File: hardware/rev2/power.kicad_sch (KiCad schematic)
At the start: 22 parts, among them J8 Battery Connection, U5 MP2664GG-xxxx-P, U6 MAX17055ETB+, U8 TPS631000DRLR

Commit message: changed layout a bit, updated footprints, did stuff
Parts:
- added C55: 100 nF, Capacitor_SMD:C_0603_1608Metric_Pad1.08x0.95mm_HandSolder, symbol Device:C
- U8: footprint TPS631000DRLR_TEX -> _footprints:TPS631000DRLR_TEX
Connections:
- net +3V3: now also C55.1
- net BATT+: now also J8.1 (Pin_1); no longer J8.3 (Pin_3)
- net BATT-: now also J8.3 (Pin_3); no longer J8.1 (Pin_1)
- net GND: now also C55.2
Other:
- moved on the sheet: J8
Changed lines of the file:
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@@
 	)
 	(junction
-		(at 215.9 49.53)
-		(diameter 0)
-		(color 0 0 0 0)
-	)
-	(junction
 		(at 137.16 130.81)
 		(diameter 0)
@@
 	)
 	(junction
+		(at 228.6 49.53)
+		(diameter 0)
+		(color 0 0 0 0)
+	)
+	(junction
 		(at 128.27 74.93)
 		(diameter 0)
 		(color 0 0 0 0)
 	)
+	(junction
+		(at 215.9 49.53)
+		(diameter 0)
+		(color 0 0 0 0)
+	)
 	(no_connect
 		(at 137.16 142.24)
@@
 	(wire
 		(pts
+			(xy 228.6 60.96) (xy 228.6 64.77)
+		)
+		(stroke
+			(width 0)
+			(type default)
+		)
+	)
+	(wire
+		(pts
 			(xy 128.27 74.93) (xy 151.13 74.93)
 		)
@@
 	(wire
 		(pts
-			(xy 215.9 49.53) (xy 222.25 49.53)
+			(xy 215.9 49.53) (xy 228.6 49.53)
 		)
 		(stroke
@@
 	(wire
 		(pts
+			(xy 228.6 49.53) (xy 228.6 53.34)
+		)
+		(stroke
+			(width 0)
+			(type default)
+		)
+	)
+	(wire
+		(pts
 			(xy 162.56 72.39) (xy 162.56 69.85)
 		)
@@
 	)
 	(symbol
+		(lib_id "power:GND")
+		(at 228.6 64.77 0)
+		(unit 1)
+		(body_style 1)
+		(exclude_from_sim no)
+		(in_bom yes)
+		(on_board yes)
+		(in_pos_files yes)
+		(dnp no)
+		(fields_autoplaced yes)
+		(property "Reference" "#PWR083"
+			(at 228.6 71.12 0)
+			(hide yes)
+			(show_name no)
+			(do_not_autoplace no)
+			(effects
+				(font
+					(size 1.27 1.27)
+				)
+			)
+		)
+		(property "Value" "GND"
+			(at 228.6 69.85 0)
+			(show_name no)
+			(do_not_autoplace no)
+			(effects
+				(font
+					(size 1.27 1.27)
+				)
+			)
+		)
+		(property "Footprint" ""
+			(at 228.6 64.77 0)
+			(hide yes)
+			(show_name no)
+			(do_not_autoplace no)
+			(effects
+				(font
+					(size 1.27 1.27)
+				)
+			)
+		)
+		(property "Datasheet" ""
+			(at 228.6 64.77 0)
+			(hide yes)
+			(show_name no)
+			(do_not_autoplace no)
+			(effects
+				(font
+					(size 1.27 1.27)
+				)
+			)
+		)
+		(property "Description" "Power symbol creates a global label with name \"GND\" , ground"
+			(at 228.6 64.77 0)
+			(hide yes)
+			(show_name no)
+			(do_not_autoplace no)
+			(effects
+				(font
+					(size 1.27 1.27)
+				)
+			)
+		)
+		(pin "1"
+		)
+		(instances
+			(project "rev2"
+				(path "/9067f306-e23c-4d77-8182-4fa2c4b88902/46484475-7656-401a-9d45-159f5e421427"
+					(reference "#PWR083")
+					(unit 1)
+				)
+			)
+		)
+	)
+	(symbol
 		(lib_id "power:+3V3")
-		(at 222.25 49.53 0)
+		(at 228.6 49.53 0)
 		(unit 1)
 		(body_style 1)
@@
 		(fields_autoplaced yes)
 		(property "Reference" "#PWR096"
-			(at 222.25 53.34 0)
+			(at 228.6 53.34 0)
 			(hide yes)
 			(show_name no)
@@
 		)
 		(property "Value" "+3V3"
-			(at 222.25 44.45 0)
+			(at 228.6 44.45 0)
 			(show_name no)
 			(do_not_autoplace no)
@@
 		)
 		(property "Footprint" ""
-			(at 222.25 49.53 0)
+			(at 228.6 49.53 0)
 			(hide yes)
 			(show_name no)
@@
 		)
 		(property "Datasheet" ""
-			(at 222.25 49.53 0)
+			(at 228.6 49.53 0)
 			(hide yes)
 			(show_name no)
@@
 		)
 		(property "Description" "Power symbol creates a global label with name \"+3V3\""
-			(at 222.25 49.53 0)
+			(at 228.6 49.53 0)
 			(hide yes)
 			(show_name no)
@@
 			)
 		)
-		(property "Footprint" "TPS631000DRLR_TEX"
+		(property "Footprint" "_footprints:TPS631000DRLR_TEX"
 			(at 162.56 49.53 0)
 			(hide yes)
@@
 	(symbol
 		(lib_id "Connector_Generic:Conn_01x03")
-		(at 93.98 127 180)
+		(at 93.98 127 0)
+		(mirror y)
 		(unit 1)
 		(body_style 1)
@@
 		(dnp no)
 		(property "Reference" "J8"
-			(at 90.678 125.7299 0)
+			(at 90.678 128.2701 0)
 			(show_name no)
 			(do_not_autoplace no)
@@
 		)
 		(property "Value" "Battery Connection"
-			(at 91.44 128.016 0)
+			(at 91.44 125.984 0)
 			(show_name no)
 			(do_not_autoplace no)
@@
 					(unit 1)
 				)
+			)
+		)
+	)
+	(symbol
+		(lib_id "Device:C")
+		(at 228.6 57.15 0)
+		(unit 1)
+		(body_style 1)
+		(exclude_from_sim no)
+		(in_bom yes)
+		(on_board yes)
+		(in_pos_files yes)
+		(dnp no)
+		(fields_autoplaced yes)
+		(property "Reference" "C55"
+			(at 232.41 55.8799 0)
+			(show_name no)
+			(do_not_autoplace no)
+			(effects
+				(font
+					(size 1.27 1.27)
+				)
+				(justify left)
+			)
+		)
+		(property "Value" "100 nF"
+			(at 232.41 58.4199 0)
+			(show_name no)
+			(do_not_autoplace no)
+			(effects
+				(font
+					(size 1.27 1.27)
+				)
+				(justify left)
+			)
+		)
+		(property "Footprint" "Capacitor_SMD:C_0603_1608Metric_Pad1.08x0.95mm_HandSolder"
+			(at 229.5652 60.96 0)
+			(hide yes)
+			(show_name no)
+			(do_not_autoplace no)
+			(effects
+				(font
+					(size 1.27 1.27)
+				)
+			)
+		)
+		(property "Datasheet" ""
+			(at 228.6 57.15 0)
+			(hide yes)
+			(show_name no)
+			(do_not_autoplace no)
+			(effects
+				(font
+					(size 1.27 1.27)
+				)
+			)
+		)
+		(property "Description" ""
+			(at 228.6 57.15 0)
+			(hide yes)
+			(show_name no)
+			(do_not_autoplace no)
+			(effects
+				(font
+					(size 1.27 1.27)
+				)
+			)
+		)
+		(property "Sim.Type" ""
+			(at 228.6 57.15 0)
+			(hide yes)
+			(show_name no)
+			(do_not_autoplace no)
+			(effects
+				(font
+					(size 1.27 1.27)
+				)
+			)
+		)
+		(property "Mouser Part Number" ""
+			(at 228.6 57.15 0)
+			(hide yes)
+			(show_name no)
+			(do_not_autoplace no)
+			(effects
+				(font
+					(size 1.27 1.27)
+				)
+			)
+		)
+		(pin "1"
+		)
+		(pin "2"
+		)
+		(instances
+			(project "rev2"
+				(path "/9067f306-e23c-4d77-8182-4fa2c4b88902/46484475-7656-401a-9d45-159f5e421427"
+					(reference "C55")
+					(unit 1)
+				)

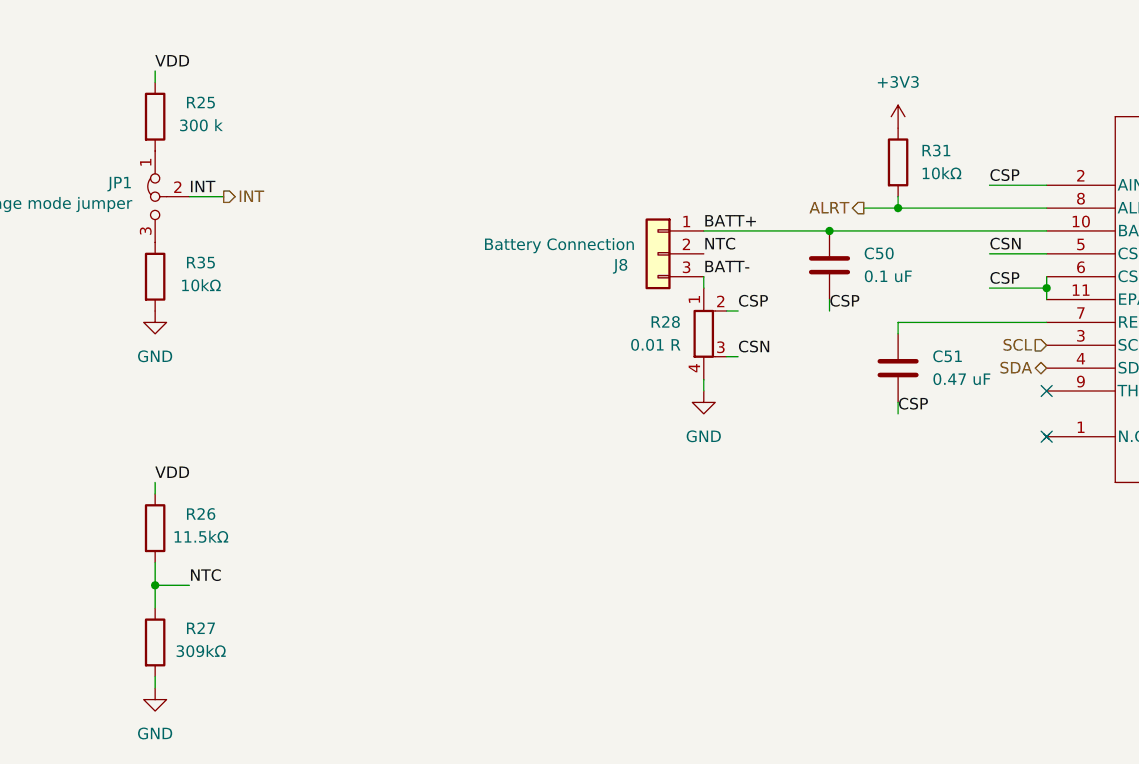
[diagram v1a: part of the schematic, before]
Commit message: fixed soldermask and silkscreen mostly
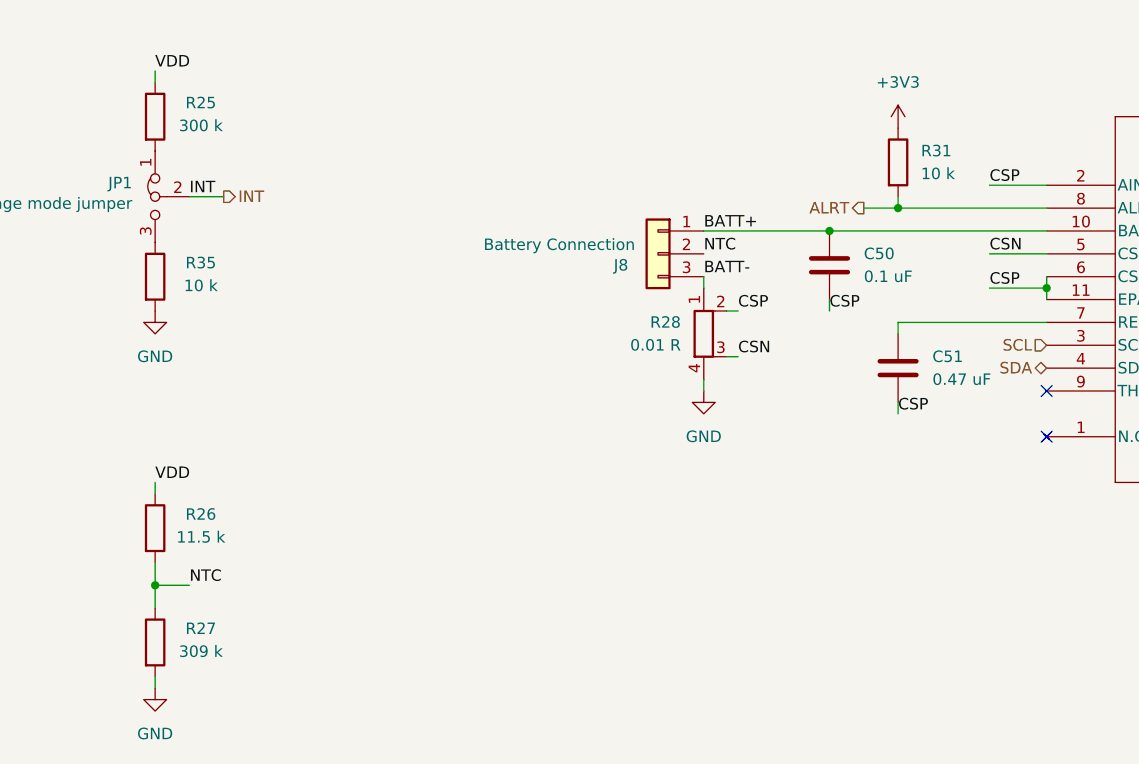
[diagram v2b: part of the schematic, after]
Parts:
- C55: Mouser Part Number (none) -> 81-GCJ188R71E104KA2D
- JP1: Mouser Part Number 200-FTR10302SS and 855-M50-1900005 -> 200-FTR10302SS
- R26: value 11.5kΩ -> 11.5 k
- R27: value 309kΩ -> 309 k
- R31, R35: value 10kΩ -> 10 k

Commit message: final edit, send to production
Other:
- company: MMCX11 -> Group 10
- title: (none) -> LoRa Based Cat Tracker
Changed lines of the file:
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@@
 	(paper "A4")
 	(title_block
-		(company "MMCX11")
+		(title "LoRa Based Cat Tracker")
+		(date "2026-04-22")
+		(rev "2.0.0")
+		(company "Group 10")
 	)
 	(junction

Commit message: unfucked vias
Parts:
- J8: footprint Connector_Molex:Molex_PicoBlade_53047-0310_1x03_P1.25mm_Vertical -> _footprints:Unfucked_Molex_PicoBlade_53047-0310_1x03_P1.25mm_Vertical
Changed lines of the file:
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@@
 			)
 		)
-		(property "Footprint" "Connector_Molex:Molex_PicoBlade_53047-0310_1x03_P1.25mm_Vertical"
+		(property "Footprint" "_footprints:Unfucked_Molex_PicoBlade_53047-0310_1x03_P1.25mm_Vertical"
 			(at 93.98 127 0)
 			(hide yes)

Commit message: changed some components that were on backorder
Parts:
- R27: Mouser Part Number 667-ERA-3AEB3093V -> 71-TNPW0603309KBEEA
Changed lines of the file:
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@@
 			)
 		)
-		(property "Datasheet" "https://industrial.panasonic.com/cdbs/www-data/pdf/RDM0000/AOA0000C307.pdf"
+		(property "Datasheet" "https://www.vishay.com/doc?28758"
 			(at 38.1 170.18 0)
 			(hide yes)
@@
 			)
 		)
-		(property "Mouser Part Number" "667-ERA-3AEB3093V"
+		(property "Mouser Part Number" "71-TNPW0603309KBEEA"
 			(at 38.1 170.18 0)
 			(hide yes)

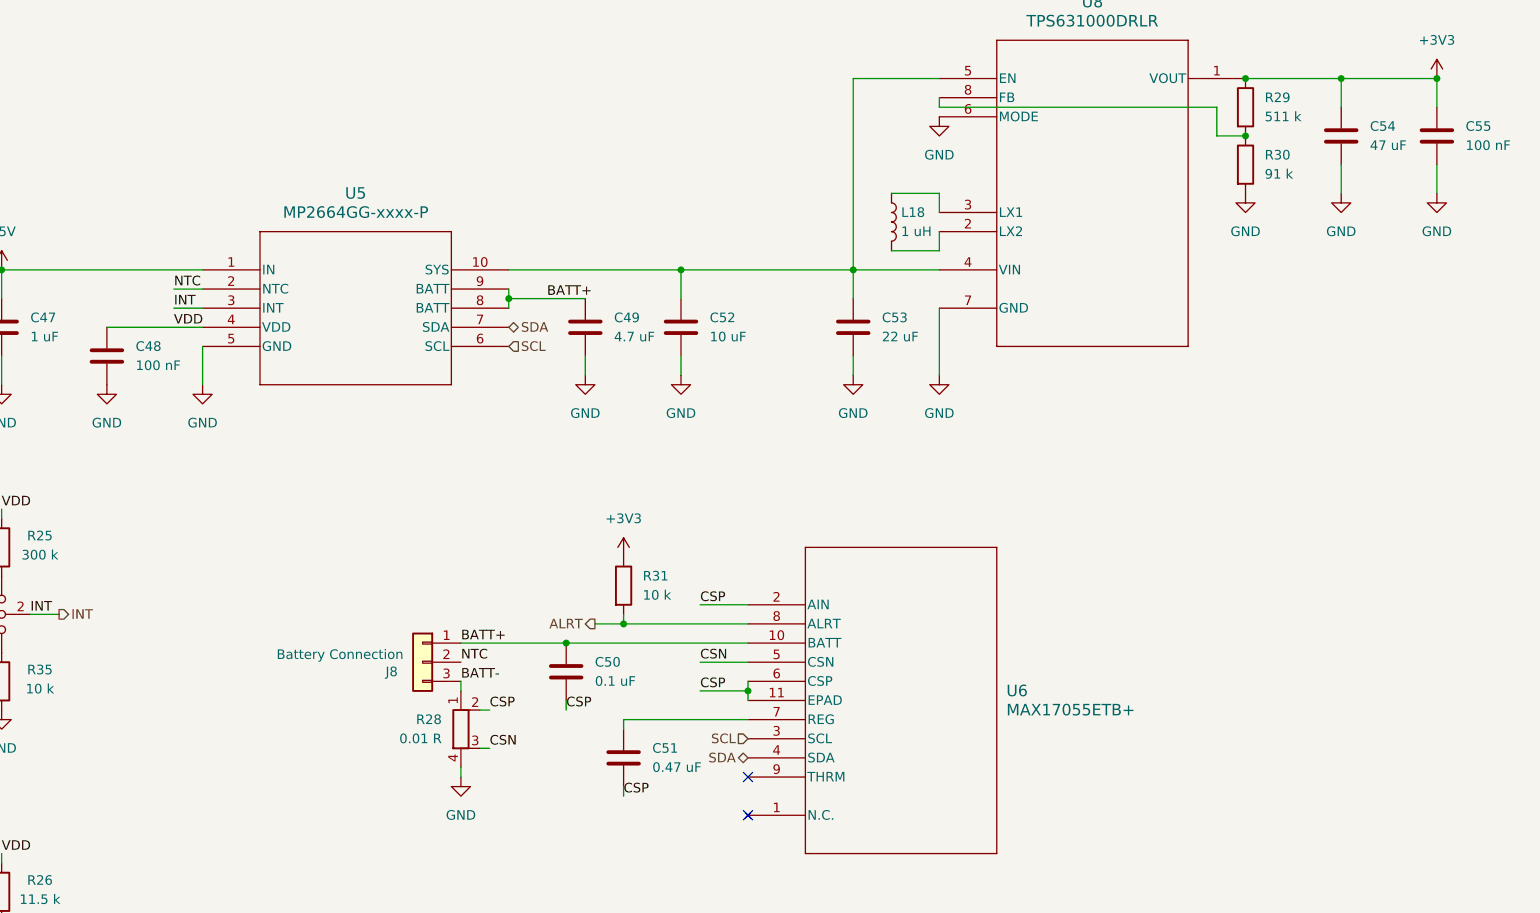
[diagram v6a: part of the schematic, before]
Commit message: changed values to be accurate to order
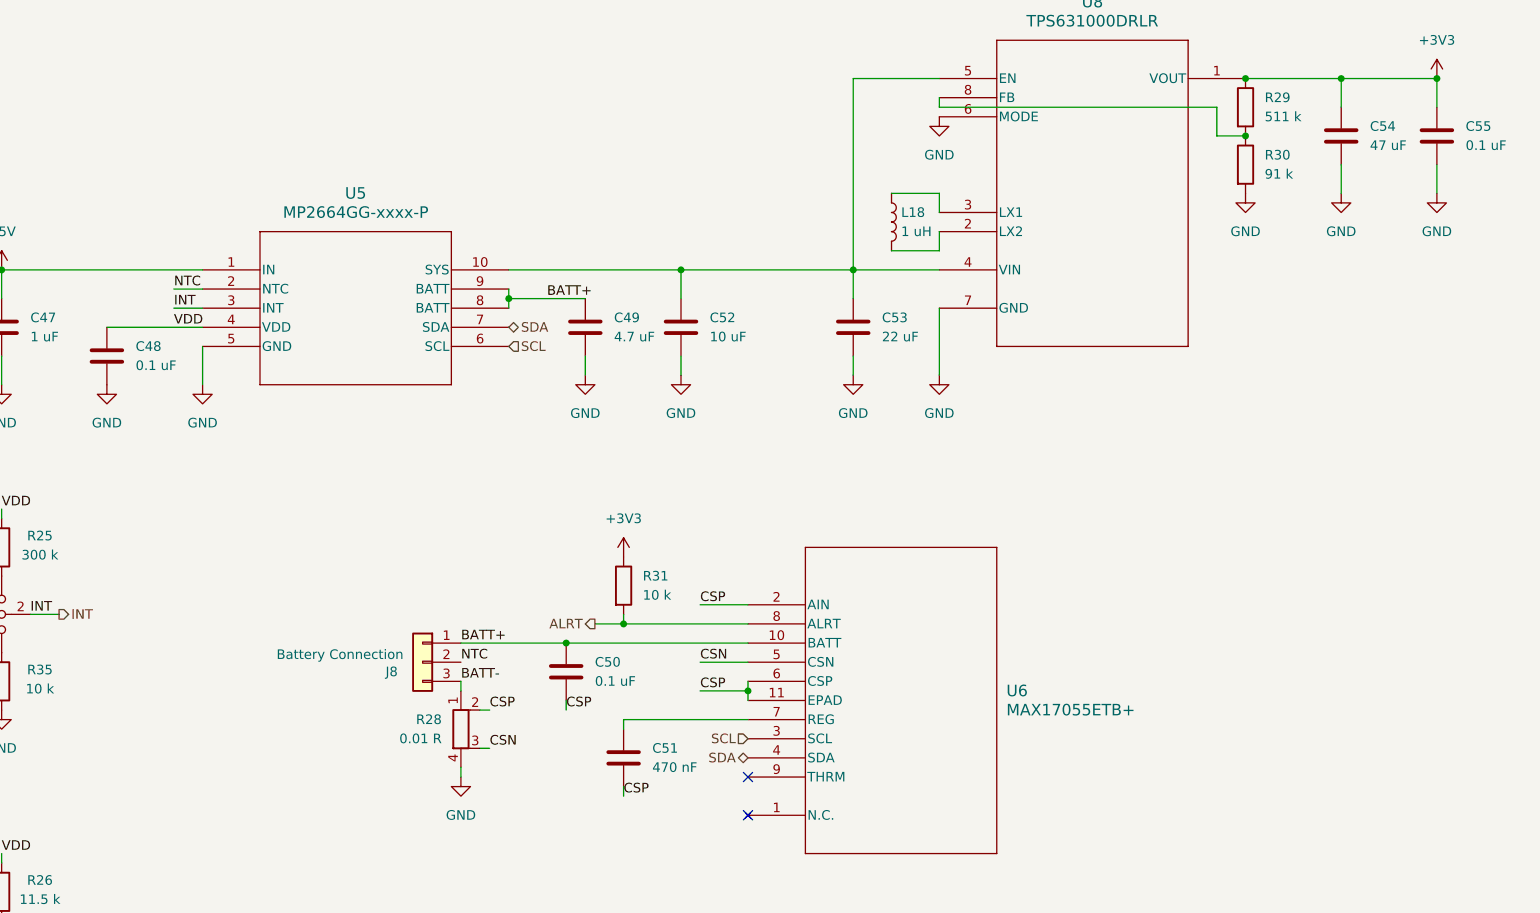
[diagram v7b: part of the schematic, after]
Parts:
- C48, C55: value 100 nF -> 0.1 uF
- C50: Mouser Part Number 81-GCJ188R71E104KA2D -> 81-GCJ188R71E104KA2D
- C51: value 0.47 uF -> 470 nF
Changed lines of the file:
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@@
 			)
 		)
-		(property "Value" "0.47 uF"
+		(property "Value" "470 nF"
 			(at 124.46 140.97 0)
 			(show_name no)
@@
 			)
 		)
-		(property "Value" "100 nF"
+		(property "Value" "0.1 uF"
 			(at 55.88 87.6299 0)
 			(show_name no)
@@
 			)
 		)
-		(property "Mouser Part Number" "81-GCJ188R71E104KA2D "
+		(property "Mouser Part Number" "81-GCJ188R71E104KA2D"
 			(at 113.03 128.27 0)
 			(hide yes)
@@
 			)
 		)
-		(property "Value" "100 nF"
+		(property "Value" "0.1 uF"
 			(at 232.41 58.4199 0)
 			(show_name no)

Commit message: made schematics more prettier among other things
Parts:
- removed U5: MP2664GG-xxxx-P, _footprints:QFN-2x2_MP2664_MNP, symbol _symbols:MP2664GG-xxxx-P
- added U5: MP2664GG-0000-P, QFN-2x2_MP2664_MNP, symbol _symbols:MP2664GG-0000-P
- U6: footprint _footprints:21-100013A_T102A2+1C_MXM -> 21-100013A_T102A2+1C_MXM
- U8: footprint _footprints:TPS631000DRLR_TEX -> TPS631000DRLR_TEX
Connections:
- net +5V: now also U5.1 (IN)
- net BATT+: now also U5.8 (BATT)
- net GND: now also U5.5 (GND)
- net INT: now also U5.3 (INT)
- net NTC: no longer R26.2, R27.1
- net SCL: now also U5.6 (SCL)
- net SDA: now also U5.7 (SDA)
- net VDD: no longer C48.1, R26.1
- net at C52.1, C53.1, U8.4 (VIN)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: now also U5.10 (SYS)
- net CSN: no longer names the net of R28.3, U6.5 (CSN)
- new net: R26.2, R27.1, U5.2 (NTC)
- new net BATT: C48.1, R26.1, U5.4 (VDD), U5.9 (BATT)
- no-connect marks 2 -> 1
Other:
- moved on the sheet: C47, C48, C49, C50, C51, C52, C53, C54, C55, J8, JP1, L18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
